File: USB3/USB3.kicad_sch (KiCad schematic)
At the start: 1 part, among them U8 TUSB8020BIPHPRQ1

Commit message: usb3 work cont
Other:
- sheet USB3clk: file USB3/USB3clk.kicad_sch -> USB3clk.kicad_sch
- sheet USB3down1: file USB3/USB3down1.kicad_sch -> USB3down1.kicad_sch
- sheet USB3down2: file USB3/USB3down2.kicad_sch -> USB3down2.kicad_sch
- sheet USB3pwr: file USB3/USB3pwr.kicad_sch -> USB3pwr.kicad_sch
- sheet USB3sw: file USB3/USB3sw.kicad_sch -> USB3sw.kicad_sch
- sheet USB3up: file USB3/USB3up.kicad_sch -> USB3up.kicad_sch
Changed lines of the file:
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@@
 			)
 		)
-		(property "Sheetfile" "USB3/USB3pwr.kicad_sch"
+		(property "Sheetfile" "USB3pwr.kicad_sch"
 			(at 167.64 117.4246 0)
 			(effects
@@
 			)
 		)
-		(property "Sheetfile" "USB3/USB3down2.kicad_sch"
+		(property "Sheetfile" "USB3down2.kicad_sch"
 			(at 83.82 117.4246 0)
 			(effects
@@
 			)
 		)
-		(property "Sheetfile" "USB3/USB3clk.kicad_sch"
+		(property "Sheetfile" "USB3clk.kicad_sch"
 			(at 139.7 117.4246 0)
 			(effects
@@
 			)
 		)
-		(property "Sheetfile" "USB3/USB3down1.kicad_sch"
+		(property "Sheetfile" "USB3down1.kicad_sch"
 			(at 55.88 117.4246 0)
 			(effects
@@
 			)
 		)
-		(property "Sheetfile" "USB3/USB3up.kicad_sch"
+		(property "Sheetfile" "USB3up.kicad_sch"
 			(at 26.67 117.4246 0)
 			(effects
@@
 			)
 		)
-		(property "Sheetfile" "USB3/USB3sw.kicad_sch"
+		(property "Sheetfile" "USB3sw.kicad_sch"
 			(at 111.76 117.4246 0)
 			(effects

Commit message: usb3 work cont
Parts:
- removed U8: TUSB8020BIPHPRQ1, PHP0048E_N_TEX, symbol 2025-10-11_06-29-10:TUSB8020BIPHPRQ1
- added U2: TUSB8041, Package_DFN_QFN:QFN-64-1EP_9x9mm_P0.5mm_EP6x6mm_ThermalVias, symbol Interface_USB:TUSB8041
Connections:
- net TEST: now also U2.49 (TEST)
- net USB_DM_DN1: now also U2.2 (USB_DM_DN1)
- net USB_DM_DN2: now also U2.10 (USB_DM_DN2)
- net USB_DM_UP: now also U2.54 (USB_DM_UP)
- net USB_DP_DN1: now also U2.1 (USB_DP_DN1)
- net USB_DP_DN2: now also U2.9 (USB_DP_DN2)
- net USB_DP_UP: now also U2.53 (USB_DP_UP)
- net USB_R1: now also U2.64 (USB_R1)
- net USB_SSRXM_DN1: now also U2.7 (USB_SSRXM_DN1)
- net USB_SSRXM_DN2: now also U2.15 (USB_SSRXM_DN2)
- net USB_SSRXM_UP: now also U2.59 (USB_SSRXM_UP)
- net USB_SSRXP_DN1: now also U2.6 (USB_SSRXP_DN1)
- net USB_SSRXP_DN2: now also U2.14 (USB_SSRXP_DN2)
- net USB_SSRXP_UP: now also U2.58 (USB_SSRXP_UP)
- net USB_SSTXM_DN1: now also U2.4 (USB_SSTXM_DN1)
- net USB_SSTXM_DN2: now also U2.12 (USB_SSTXM_DN2)
- net USB_SSTXM_UP: now also U2.56 (USB_SSTXM_UP)
- net USB_SSTXP_DN1: now also U2.3 (USB_SSTXP_DN1)
- net USB_SSTXP_DN2: now also U2.11 (USB_SSTXP_DN2)
- net USB_SSTXP_UP: now also U2.55 (USB_SSTXP_UP)
- net USB_VBUS: now also U2.48 (USB_VBUS)
- net VDD: now also U2.13 (VDD), U2.21 (VDD), U2.28 (VDD), U2.31 (VDD), U2.5 (VDD), U2.51 (VDD), U2.57 (VDD), U2.8 (VDD)
- net VDD33: now also U2.16 (VDD33), U2.34 (VDD33), U2.52 (VDD33), U2.63 (VDD33)
- net XI: now also U2.62 (XI)
- net XO: now also U2.61 (XO)
- new net AUTOENz/HS_SUSPEND: U2.45 (AUTOENz/HS_SUSPEND)
- new net FULLPWRMGMTz/SMBA1/SS_UP: U2.40 (FULLPWRMGMTz/SMBA1/SS_UP)
- new net GANGED/SMBA2/HS_UP: U2.42 (GANGED/SMBA2/HS_UP)
- new net GND: U2.65 (VSS)
- new net GRSTz: U2.50 (GRSTz)
- new net OVERCUR1z: U2.46 (OVERCUR1z)
- new net OVERCUR2z: U2.47 (OVERCUR2z)
- new net OVERCUR3z: U2.44 (OVERCUR3z)
- new net OVERCUR4z: U2.43 (OVERCUR4z)
- new net PWRCTL1/BATEN1: U2.36 (PWRCTL1/BATEN1)
- new net PWRCTL2/BATEN2: U2.35 (PWRCTL2/BATEN2)
- new net PWRCTL3/BATEN3: U2.33 (PWRCTL3/BATEN3)
- new net PWRCTL4/BATEN4: U2.32 (PWRCTL4/BATEN4)
- new net PWRCTL_POL: U2.41 (PWRCTL_POL)
- new net SCL/SMBCLK: U2.38 (SCL/SMBCLK)
- new net SDA/SMBDAT: U2.37 (SDA/SMBDAT)
- new net SMBUSz/SS_SUSPEND: U2.39 (SMBUSz/SS_SUSPEND)
- new net USB_DM_DN3: U2.18 (USB_DM_DN3)
- new net USB_DM_DN4: U2.25 (USB_DM_DN4)
- new net USB_DP_DN3: U2.17 (USB_DP_DN3)
- new net USB_DP_DN4: U2.24 (USB_DP_DN4)
- new net USB_SSRXM_DN3: U2.23 (USB_SSRXM_DN3)
- new net USB_SSRXM_DN4: U2.30 (USB_SSRXM_DN4)
- new net USB_SSRXP_DN3: U2.22 (USB_SSRXP_DN3)
- new net USB_SSRXP_DN4: U2.29 (USB_SSRXP_DN4)
- new net USB_SSTXM_DN3: U2.20 (USB_SSTXM_DN3)
- new net USB_SSTXM_DN4: U2.27 (USB_SSTXM_DN4)
- new net USB_SSTXP_DN3: U2.19 (USB_SSTXP_DN3)
- new net USB_SSTXP_DN4: U2.26 (USB_SSTXP_DN4)

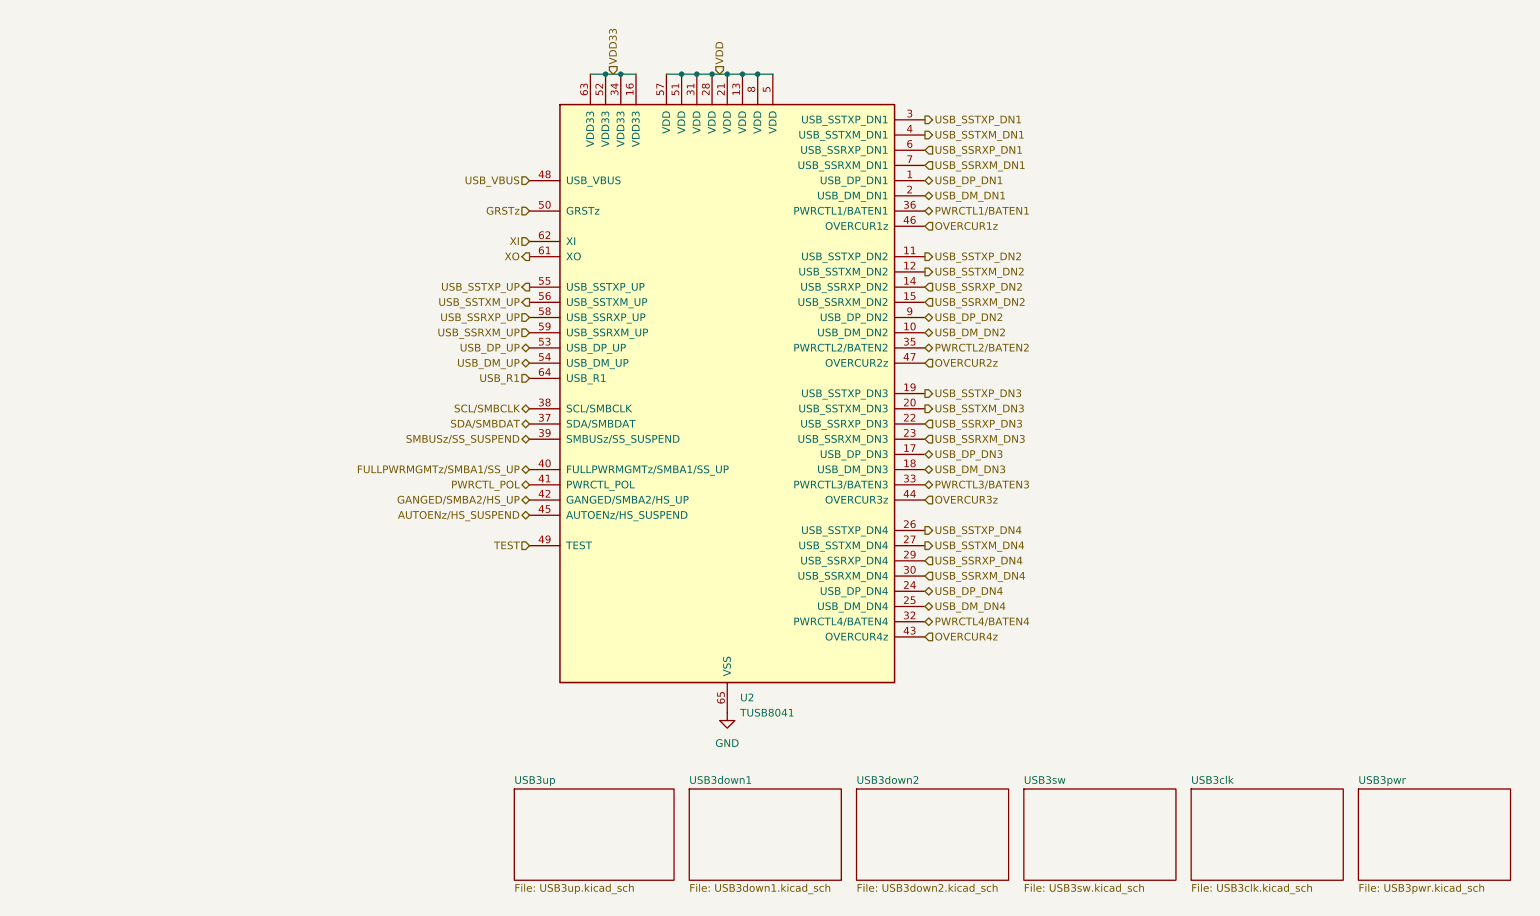
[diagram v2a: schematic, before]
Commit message: usb3up done, usb3down begun
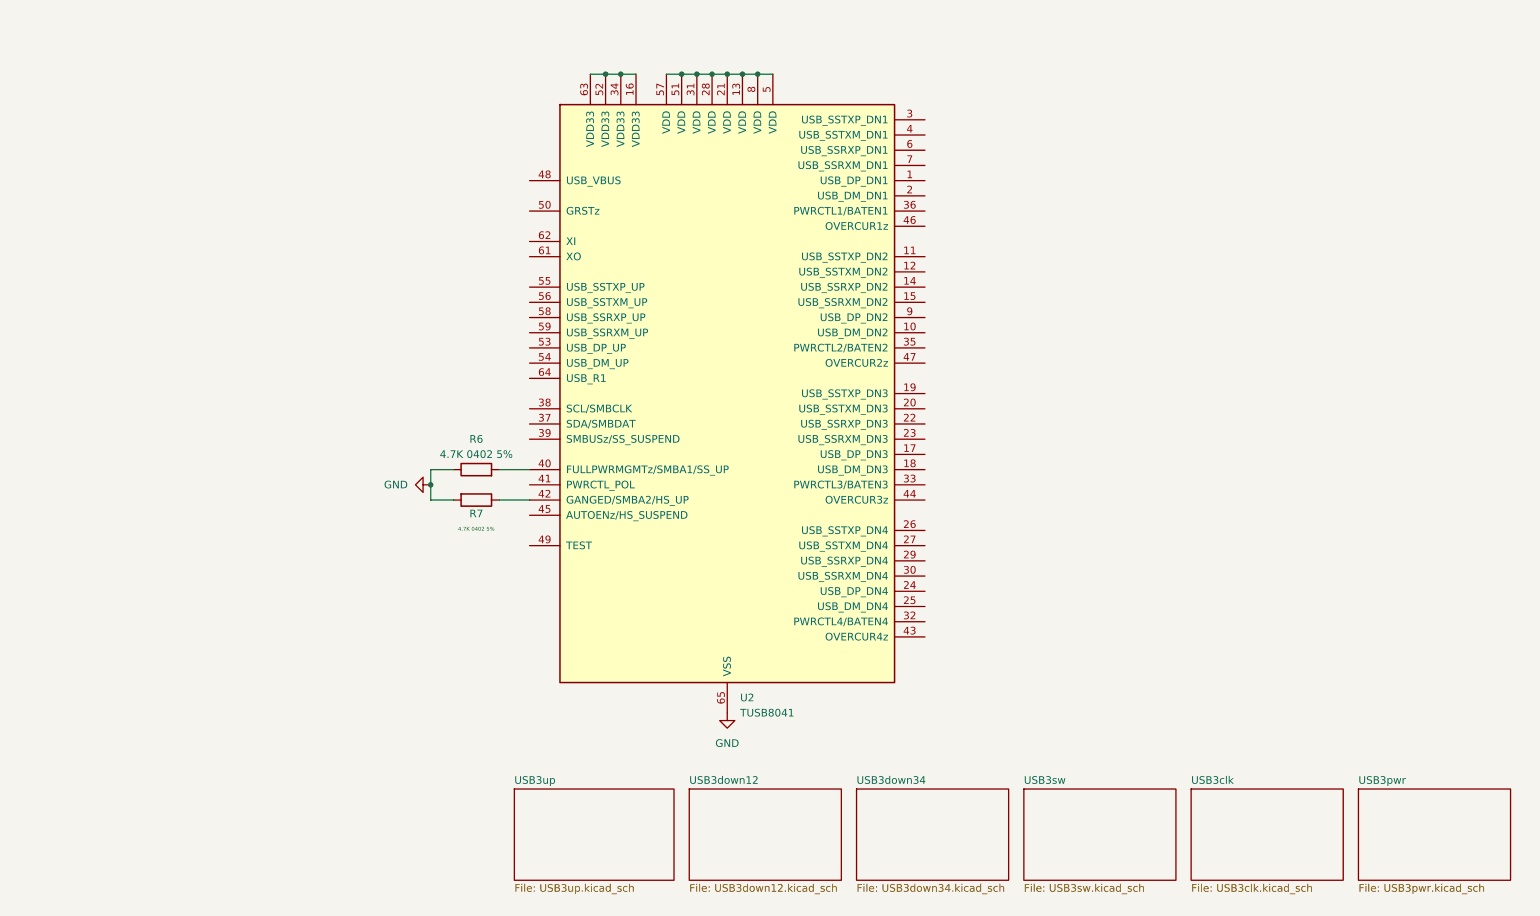
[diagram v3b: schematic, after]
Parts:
- added R6, R7: 4.7K 0402 5%, symbol Device:R
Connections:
- net GND: now also R6.1, R7.2
- net AUTOENz/HS_SUSPEND: no longer names the net of U2.45 (AUTOENz/HS_SUSPEND)
- net FULLPWRMGMTz/SMBA1/SS_UP: no longer names the net of U2.40 (FULLPWRMGMTz/SMBA1/SS_UP)
- net FULLPWRMGMTz/SMBA1/SS_UP: now also R6.2
- net GANGED/SMBA2/HS_UP: no longer names the net of U2.42 (GANGED/SMBA2/HS_UP)
- net GANGED/SMBA2/HS_UP: now also R7.1
- net GRSTz: no longer names the net of U2.50 (GRSTz)
- net OVERCUR1z: no longer names the net of U2.46 (OVERCUR1z)
- net OVERCUR2z: no longer names the net of U2.47 (OVERCUR2z)
- net OVERCUR3z: no longer names the net of U2.44 (OVERCUR3z)
- net OVERCUR4z: no longer names the net of U2.43 (OVERCUR4z)
- net PWRCTL1/BATEN1: no longer names the net of U2.36 (PWRCTL1/BATEN1)
- net PWRCTL2/BATEN2: no longer names the net of U2.35 (PWRCTL2/BATEN2)
- net PWRCTL3/BATEN3: no longer names the net of U2.33 (PWRCTL3/BATEN3)
- net PWRCTL4/BATEN4: no longer names the net of U2.32 (PWRCTL4/BATEN4)
- net PWRCTL_POL: no longer names the net of U2.41 (PWRCTL_POL)
- net SCL/SMBCLK: no longer names the net of U2.38 (SCL/SMBCLK)
- net SDA/SMBDAT: no longer names the net of U2.37 (SDA/SMBDAT)
- net SMBUSz/SS_SUSPEND: no longer names the net of U2.39 (SMBUSz/SS_SUSPEND)
- net TEST: no longer names the net of U2.49 (TEST)
- net USB_DM_DN1: no longer names the net of U2.2 (USB_DM_DN1)
- net USB_DM_DN2: no longer names the net of U2.10 (USB_DM_DN2)
- net USB_DM_DN3: no longer names the net of U2.18 (USB_DM_DN3)
- net USB_DM_DN4: no longer names the net of U2.25 (USB_DM_DN4)
- net USB_DM_UP: no longer names the net of U2.54 (USB_DM_UP)
- net USB_DP_DN1: no longer names the net of U2.1 (USB_DP_DN1)
- net USB_DP_DN2: no longer names the net of U2.9 (USB_DP_DN2)
- net USB_DP_DN3: no longer names the net of U2.17 (USB_DP_DN3)
- net USB_DP_DN4: no longer names the net of U2.24 (USB_DP_DN4)
- net USB_DP_UP: no longer names the net of U2.53 (USB_DP_UP)
- net USB_R1: no longer names the net of U2.64 (USB_R1)
- net USB_SSRXM_DN1: no longer names the net of U2.7 (USB_SSRXM_DN1)
- net USB_SSRXM_DN2: no longer names the net of U2.15 (USB_SSRXM_DN2)
- net USB_SSRXM_DN3: no longer names the net of U2.23 (USB_SSRXM_DN3)
- net USB_SSRXM_DN4: no longer names the net of U2.30 (USB_SSRXM_DN4)
- net USB_SSRXM_UP: no longer names the net of U2.59 (USB_SSRXM_UP)
- net USB_SSRXP_DN1: no longer names the net of U2.6 (USB_SSRXP_DN1)
- net USB_SSRXP_DN2: no longer names the net of U2.14 (USB_SSRXP_DN2)
- net USB_SSRXP_DN3: no longer names the net of U2.22 (USB_SSRXP_DN3)
- net USB_SSRXP_DN4: no longer names the net of U2.29 (USB_SSRXP_DN4)
- net USB_SSRXP_UP: no longer names the net of U2.58 (USB_SSRXP_UP)
- net USB_SSTXM_DN1: no longer names the net of U2.4 (USB_SSTXM_DN1)
- net USB_SSTXM_DN2: no longer names the net of U2.12 (USB_SSTXM_DN2)
- net USB_SSTXM_DN3: no longer names the net of U2.20 (USB_SSTXM_DN3)
- net USB_SSTXM_DN4: no longer names the net of U2.27 (USB_SSTXM_DN4)
- net USB_SSTXM_UP: no longer names the net of U2.56 (USB_SSTXM_UP)
- net USB_SSTXP_DN1: no longer names the net of U2.3 (USB_SSTXP_DN1)
- net USB_SSTXP_DN2: no longer names the net of U2.11 (USB_SSTXP_DN2)
- net USB_SSTXP_DN3: no longer names the net of U2.19 (USB_SSTXP_DN3)
- net USB_SSTXP_DN4: no longer names the net of U2.26 (USB_SSTXP_DN4)
- net USB_SSTXP_UP: no longer names the net of U2.55 (USB_SSTXP_UP)
- net USB_VBUS: no longer names the net of U2.48 (USB_VBUS)
- net VDD: no longer names the net of U2.13 (VDD), U2.21 (VDD), U2.28 (VDD), U2.31 (VDD), U2.5 (VDD), U2.51 (VDD), U2.57 (VDD), U2.8 (VDD)
- net VDD33: no longer names the net of U2.16 (VDD33), U2.34 (VDD33), U2.52 (VDD33), U2.63 (VDD33)
- net XI: no longer names the net of U2.62 (XI)
- net XO: no longer names the net of U2.61 (XO)
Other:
- sheet USB3down1 renamed USB3down12
- sheet USB3down2 renamed USB3down34
- sheet USB3down12: file USB3down1.kicad_sch -> USB3down12.kicad_sch
- sheet USB3down34: file USB3down2.kicad_sch -> USB3down34.kicad_sch

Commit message: usb3 down done
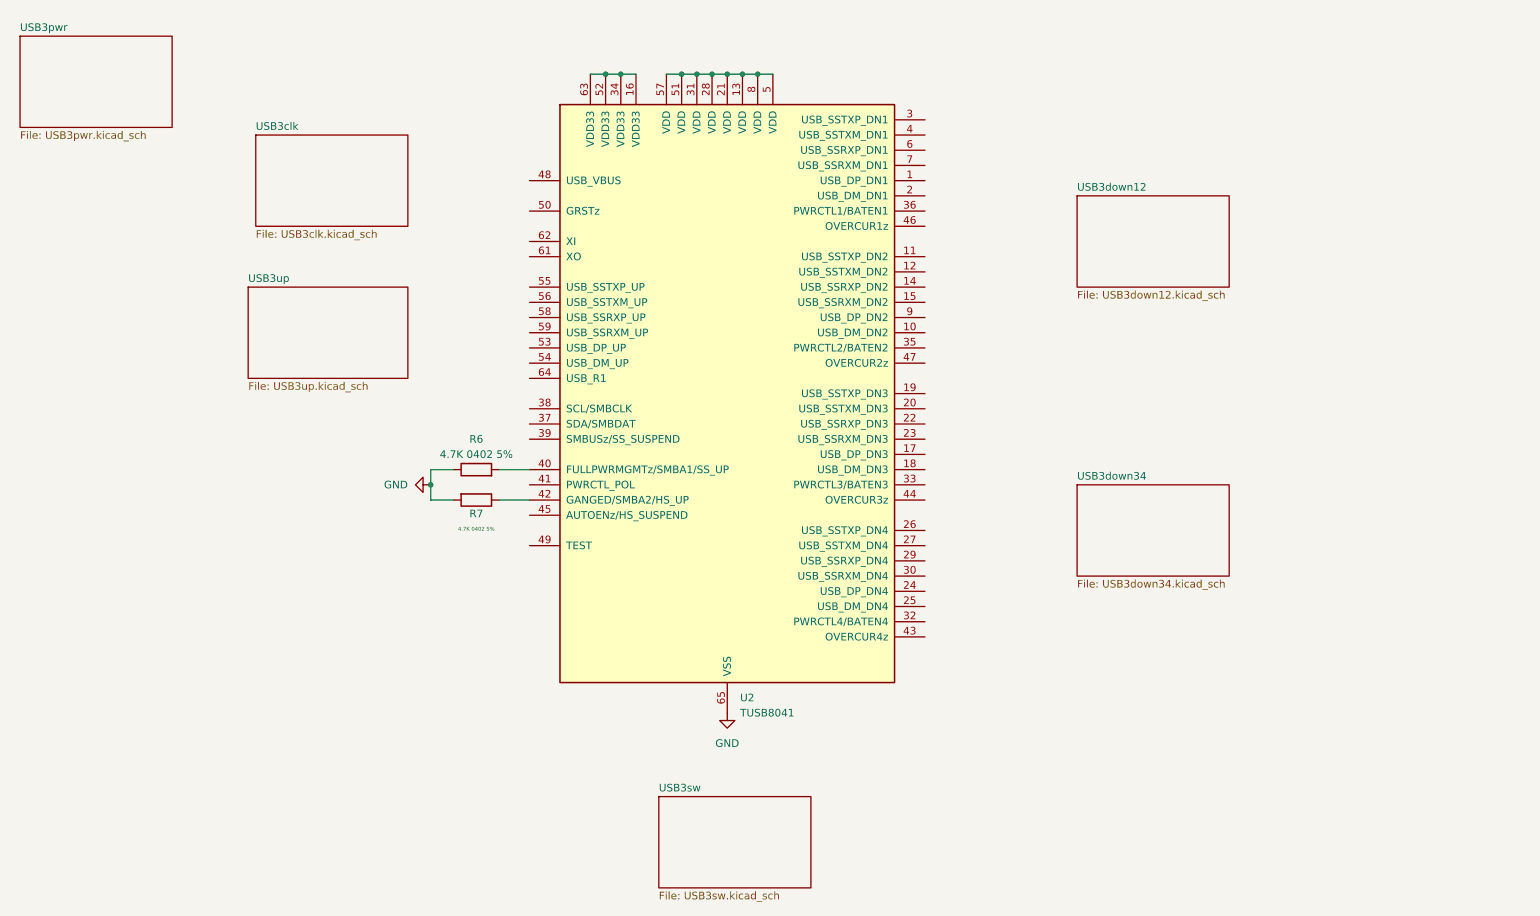
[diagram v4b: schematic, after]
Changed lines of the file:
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@@
 	)
 	(sheet
-		(at 251.46 142.24)
+		(at 27.94 16.51)
 		(size 25.4 15.24)
 		(exclude_from_sim no)
@@
 		)
 		(property "Sheetname" "USB3pwr"
-			(at 251.46 141.5284 0)
+			(at 27.94 15.7984 0)
 			(effects
 				(font
@@
 		)
 		(property "Sheetfile" "USB3pwr.kicad_sch"
-			(at 251.46 158.0646 0)
+			(at 27.94 32.3346 0)
 			(effects
 				(font
@@
 	)
 	(sheet
-		(at 167.64 142.24)
+		(at 204.47 91.44)
 		(size 25.4 15.24)
 		(exclude_from_sim no)
@@
 		)
 		(property "Sheetname" "USB3down34"
-			(at 167.64 141.5284 0)
+			(at 204.47 90.7284 0)
 			(effects
 				(font
@@
 		)
 		(property "Sheetfile" "USB3down34.kicad_sch"
-			(at 167.64 158.0646 0)
+			(at 204.47 107.2646 0)
 			(effects
 				(font
@@
 	)
 	(sheet
-		(at 223.52 142.24)
+		(at 67.31 33.02)
 		(size 25.4 15.24)
 		(exclude_from_sim no)
@@
 		)
 		(property "Sheetname" "USB3clk"
-			(at 223.52 141.5284 0)
+			(at 67.31 32.3084 0)
 			(effects
 				(font
@@
 		)
 		(property "Sheetfile" "USB3clk.kicad_sch"
-			(at 223.52 158.0646 0)
+			(at 67.31 48.8446 0)
 			(effects
 				(font
@@
 	)
 	(sheet
-		(at 139.7 142.24)
+		(at 204.47 43.18)
 		(size 25.4 15.24)
 		(exclude_from_sim no)
@@
 		)
 		(property "Sheetname" "USB3down12"
-			(at 139.7 141.5284 0)
+			(at 204.47 42.4684 0)
 			(effects
 				(font
@@
 		)
 		(property "Sheetfile" "USB3down12.kicad_sch"
-			(at 139.7 158.0646 0)
+			(at 204.47 59.0046 0)
 			(effects
 				(font
@@
 	)
 	(sheet
-		(at 110.49 142.24)
+		(at 66.04 58.42)
 		(size 26.67 15.24)
 		(exclude_from_sim no)
@@
 		)
 		(property "Sheetname" "USB3up"
-			(at 110.49 141.5284 0)
+			(at 66.04 57.7084 0)
 			(effects
 				(font
@@
 		)
 		(property "Sheetfile" "USB3up.kicad_sch"
-			(at 110.49 158.0646 0)
+			(at 66.04 74.2446 0)
 			(effects
 				(font
@@
 	)
 	(sheet
-		(at 195.58 142.24)
+		(at 134.62 143.51)
 		(size 25.4 15.24)
 		(exclude_from_sim no)
@@
 		)
 		(property "Sheetname" "USB3sw"
-			(at 195.58 141.5284 0)
+			(at 134.62 142.7984 0)
 			(effects
 				(font
@@
 		)
 		(property "Sheetfile" "USB3sw.kicad_sch"
-			(at 195.58 158.0646 0)
-			(effects
-				(font
+			(at 134.62 159.3346 0)
+			(effects
+				(font
